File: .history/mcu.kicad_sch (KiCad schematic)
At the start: 175 parts, among them IC1 SKY13373-460LF, IC2 AD8318ACPZ-REEL7, IC3 AD8318ACPZ-REEL7, IC4 TPS2121RUXT, IC5 MAX17048G+T10, IC6 MAX17048G+T10, IC7 TCA9543ADR, IC8 MAX16150AUT+T, J1 Interface, J2 Connector, J4 JST_MAIN, M1 Motor_DC, Q1 AO3400A, Q4 AO3401A, SW1 POWER, U1 ESP32-S3-WROOM-2, U10 DRV2605LDGS, U11 LC76G, U12 RV-3028-C7, U13 SA818S, U14 INA219BxDCN, U15 INA219BxDCN, U16 INA219BxDCN, U2 TCD-10-23BDX+, U21 WM8960, U23 E22-900M30S, U24 E22-170M30S, U3 MCP23017x-x-ML, U4 BMP390, U5 IS31FL3218-QF, U6 LSM6DSOXTR, U7 BQ24075RGT, U8 MCP23017x-x-ML, U9 BQ24075RGT

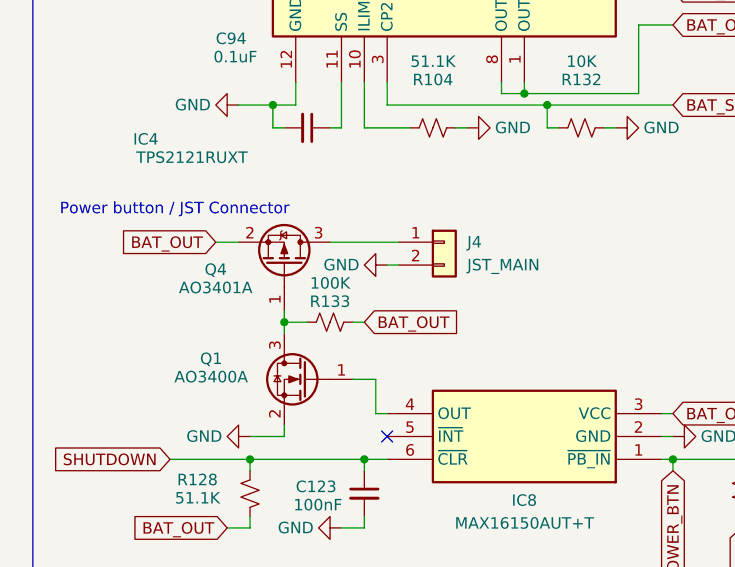
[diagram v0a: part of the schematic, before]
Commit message: Added power button latch logic, consumption logic, RTC
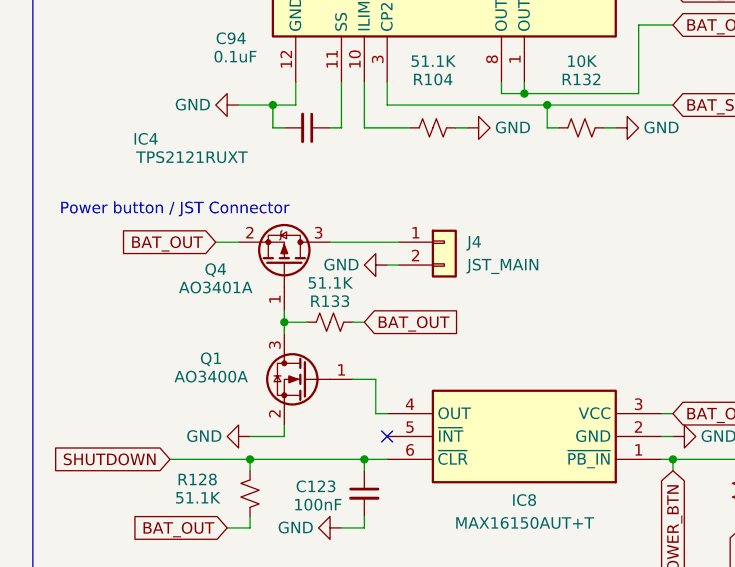
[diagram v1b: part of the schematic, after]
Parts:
- R133: value 100K -> 51.1K
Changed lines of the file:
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@@
 			)
 		)
-		(property "Value" "100K"
+		(property "Value" "51.1K"
 			(at 45.72 270.002 90)
 			(show_name no)

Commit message: Routed secondary PCB with Power and charging managment, and routed FPC Connector
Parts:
- removed J2: Connector, Connector_FFC-FPC:Amphenol_F32R-1A7x1-11029_1x29-1MP_P0.5mm_Horizontal, symbol Connector_Generic:Conn_02x15_Counter_Clockwise
- removed R80: 10K, Resistor_SMD:R_0402_1005Metric, symbol Device:R_Small_US
- added C125, C128, C130, C131, C132, C133, C134: 100nF, Capacitor_SMD:C_0402_1005Metric, symbol Device:C_Small
- added C126, C127, C129: 2.2uF, Capacitor_SMD:C_0402_1005Metric, symbol Device:C_Small
- added FB5, FB6: 600R @100MHz 500mA, Inductor_SMD:L_0402_1005Metric, symbol Device:FerriteBead
- added FB7: 600R @100MHz 4A, Inductor_SMD:L_0402_1005Metric, symbol Device:FerriteBead
- added IC10: TPS22965NTDSGRQ1, SON50P200X200X80-9N, symbol PTCR-V5:TPS22965NTDSGRQ1
- added IC9: SN74LVC1G74RSE2, SN74LVC1G74RSE2, symbol PTCR-V5:SN74LVC1G74RSE2
- added J3: Board_1, Connector_FFC-FPC:Molex_502244-3330_1x33-1MP_P0.5mm_Horizontal, symbol Connector_Generic:Conn_02x16_Counter_Clockwise
- added Q2, Q3: AO3400A, Package_TO_SOT_SMD:SOT-23, symbol Transistor_FET:AO3400A
- added R134: 5K, Resistor_SMD:R_0402_1005Metric, symbol Device:R_Small_US
- added R135: 1K, Resistor_SMD:R_0402_1005Metric, symbol Device:R_Small_US
- added R136, R138: 10K 0.1%, Resistor_SMD:R_0402_1005Metric, symbol Device:R_Small_US
- added R137: 5.6K 0.1%, Resistor_SMD:R_0402_1005Metric, symbol Device:R_Small_US
- added R139, R140: 10K, Resistor_SMD:R_0402_1005Metric, symbol Device:R_Small_US
- added TP7: +3V3_RF, TestPoint:TestPoint_Pad_D1.0mm, symbol Connector:TestPoint
- added TP8: +5V_RF, TestPoint:TestPoint_Pad_D1.0mm, symbol Connector:TestPoint
- added U17: MCP4725xxx-xCH, Package_TO_SOT_SMD:SOT-23-6, symbol Analog_DAC:MCP4725xxx-xCH
- added U18: TLV3501AIDBV, Package_TO_SOT_SMD:SOT-23-6, symbol Comparator:TLV3501AIDBV
- FB1: value 600R @100MHz 1A -> 600R @100MHz 2A
- IC7: footprint SOIC127P600X175-14N -> PTCR:SOIC127P600X175-14N
- R100: value 13.7K -> 16K
- R101: value 23.7K -> 16K
- R133: value 51.1K -> 100K
- R96: value 1K -> 10K
- R97: value 1K -> 5.6K 0.1%
- TP5: value +3V3_RF -> +5V_RF
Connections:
- net +3V3: now also C37.1, R129.2, U21.10 (DBVDD), C125.2, C126.2, C127.2, C128.2, C129.2, C130.2, FB5.2, FB7.1, IC10.4 (VBIAS), IC9.1 (~{PRE}), IC9.6 (D), IC9.8 (VCC), J3.1 (Pin_1), J3.2 (Pin_2), J3.3 (Pin_3), R134.1, R140.1, U17.3 (VDD), U18.4 (V+); no longer FB3.2, R131.1, U16.2 (IN-)
- net +3V3_RF: now also FB5.1, TP7.1; no longer C104.1, C105.1, C106.2, C107.2, C109.1, C110.1, C113.2, C114.2, FB3.1, IC2.3 (VPSI_2), IC2.4 (VPSI), IC2.9 (VPSO), IC3.3 (VPSI_2), IC3.4 (VPSI), IC3.9 (VPSO), R92.2, TP5.1
- net +5V: now also FB3.2, FB6.2, J3.25 (Pin_25), J3.26 (Pin_26), J3.27 (Pin_27)
- net AD8318_EN: now also Q2.1 (G); no longer IC3.16 (ENBL), R92.1
- net BAT1_CHG: no longer U8.18 (GPA1)
- net BAT1_PGOOD: no longer U8.17 (GPA0)
- net BAT2_CHG: no longer U8.20 (GPA3)
- net BAT2_PGOOD: no longer U8.19 (GPA2)
- net BATS_INT: no longer U8.21 (GPA4)
- net BATS_RESET: no longer U8.22 (GPA5)
- net BAT_OUT: no longer R129.2, U11.6 (V_BCKP)
- net BAT_SEL: no longer U8.24 (GPA7)
- net BAT_VAL: now also R134.2; no longer U8.23 (GPA6)
- net BUTTON0: now also J3.15 (Pin_15)
- net BUTTON1: now also J3.14 (Pin_14)
- net FWD: now also C134.2, R137.1, R138.1; no longer R96.1
- net GND: now also R96.2, C125.1, C126.1, C127.1, C128.1, C129.1, C130.1, C131.1, C132.1, C133.1, C134.1, IC10.5 (GND), IC10.9 (EP), IC9.4 (GND), J3.22 (Pin_22), J3.23 (Pin_23), J3.24 (Pin_24), J3.28 (Pin_28), J3.29 (Pin_29), J3.30 (Pin_30), J3.31 (Pin_31), Q2.2 (S), Q3.2 (S), R136.2, R138.2, R139.1, U17.2 (VSS), U17.6 (A0), U18.2 (V-)
- net INTA_MCP_1: now also U3.16 (INTA)
- net INTA_MCP_2: now also U8.16 (INTA)
- net INT_RTC: now also D8.1 (K), U3.22 (GPA5); no longer D8.2 (A), U3.24 (GPA7)
- net JOYSTICK_X: now also J3.12 (Pin_12)
- net JOYSTICK_Y: now also J3.13 (Pin_13)
- net MISO: now also U23.16 (MISO), U24.16 (MISO); no longer U23.17 (MOSI), U24.17 (MOSI)
- net MOSI: now also U23.17 (MOSI), U24.17 (MOSI); no longer U23.16 (MISO), U24.16 (MISO)
- net MOTOR: now also R96.1
- net POWER_BTN: now also J3.16 (Pin_16); no longer D8.1 (K), IC8.1 (~{PB_IN}), R129.1, SW1.1
- net REV: now also C133.2, R136.1, U18.1 (-)
- net ROT_ENC1: now also J3.10 (Pin_10)
- net ROT_ENC2: now also J3.11 (Pin_11)
- net SC0: now also IC5.7 (SCL); no longer IC5.8 (SDA)
- net SC1: now also IC6.7 (SCL); no longer IC6.8 (SDA)
- net SCL: now also J3.9 (Pin_9), U17.5 (SCL)
- net SD0: now also IC5.8 (SDA); no longer IC5.7 (SCL)
- net SD1: now also IC6.8 (SDA); no longer IC6.7 (SCL)
- net SDA: now also J3.8 (Pin_8), U17.4 (SDA)
- net SDB: no longer R98.1, U3.19 (GPA2)
- net SHUTDOWN: now also Q3.1 (G); no longer C123.1, IC8.6 (~{CLR}), R128.2, U8.26 (GPB1)
- net VIN: now also IC10.7 (VOUT_1), IC10.8 (VOUT_2); no longer C95.1, C96.1, R127.1, U13.8 (VBAT), U14.2 (IN-)
- net at IC2.6 (VOUT), IC2.7 (VSET): now also R137.2; no longer R96.2
- net SHDN_COMP: now reaches U8.1 (GPB4)
- net SHDN_COMP: now also R139.2, U18.6 (SHDN)
- net BAT_SEL_1: now reaches U8.2 (GPB5)
- net BAT_SEL_1: now also J3.18 (Pin_18)
- net RF_FAULT: now reaches U8.27 (GPB2)
- net RF_FAULT: now also IC9.3 (Q)
- net RF_FAULT_RESET: now reaches U8.28 (GPB3)
- net RF_FAULT_RESET: now also IC9.2 (~{CLR}), R140.2
- net D1B_A renamed D1G
- net D1G_A renamed D1B
- net D1R_A renamed D1R
- net D2B_A renamed D2G
- net D2G_A renamed D2B
- net D2R_A renamed D2R
- net D3B_A renamed D3G
- net D3G_A renamed D3B
- net D3R_A renamed D3R
- net D4B_A renamed D4G
- net D4G_A renamed D4B
- net D4R_A renamed D4R
- net D5B_A renamed D5G
- net D5G_A renamed D5B
- net D5R_A renamed D5R
- net D6B_A renamed D6G
- net D6G_A renamed D6B
- net D6R_A renamed D6R
- removed net INTA_MCP: U3.16 (INTA), U8.16 (INTA)
- new net: R135.2, U17.1 (VOUT)
- new net: C123.1, IC8.6 (~{CLR}), Q3.3 (D), R128.2
- new net: IC3.16 (ENBL), Q2.3 (D), R92.1
- new net: FB7.2, R131.1, U16.2 (IN-)
- new net: C132.2, IC10.6 (CT)
- new net +3V3_RADIO_OUT: IC10.1 (VIN_1), IC10.2 (VIN_2), R127.1, U14.2 (IN-)
- new net +5V_RADIO: C95.1, C96.1, FB6.1, TP8.1, U13.8 (VBAT)
- new net +5V_RF: C104.1, C105.1, C106.2, C107.2, C109.1, C110.1, C113.2, C114.2, FB3.1, IC2.3 (VPSI_2), IC2.4 (VPSI), IC2.9 (VPSO), IC3.3 (VPSI_2), IC3.4 (VPSI), IC3.9 (VPSO), R92.2, TP5.1
- new net BAT1_CHG_1: J3.5 (Pin_5), U8.18 (GPA1)
- new net BAT1_PGOOD_1: J3.4 (Pin_4), U8.17 (GPA0)
- new net BAT2_CHG_1: J3.7 (Pin_7), U8.20 (GPA3)
- new net BAT2_PGOOD_1: J3.6 (Pin_6), U8.19 (GPA2)
- new net BATS_INT_1: J3.17 (Pin_17), U8.21 (GPA4)
- new net BATS_RESET_1: J3.21 (Pin_21), U8.22 (GPA5)
- new net BAT_VAL_1: J3.20 (Pin_20), U8.23 (GPA6)
- new net CLK_SWITCH: IC9.7 (CLK), U18.5
- new net POWER_BTN_B: D8.2 (A), IC8.1 (~{PB_IN}), R129.1, SW1.1
- new net SDB_1: J3.32 (Pin_32), R98.1, U3.19 (GPA2)
- new net SHUTDOWN_1: J3.19 (Pin_19), U8.26 (GPB1)
- new net TPS22965_ON: IC10.3 (ON), IC9.5 (~{Q})
- new net VOUT_ADC: C131.2, R135.1, U18.3 (+)
- no-connect marks 32 -> 33
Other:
- note added: "SA818S"
- moved on the sheet: AE6, C100, C26, C27, C28, C29, C30, C31, C40, C95, C96, C99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
